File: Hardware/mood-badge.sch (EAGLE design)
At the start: 92 parts

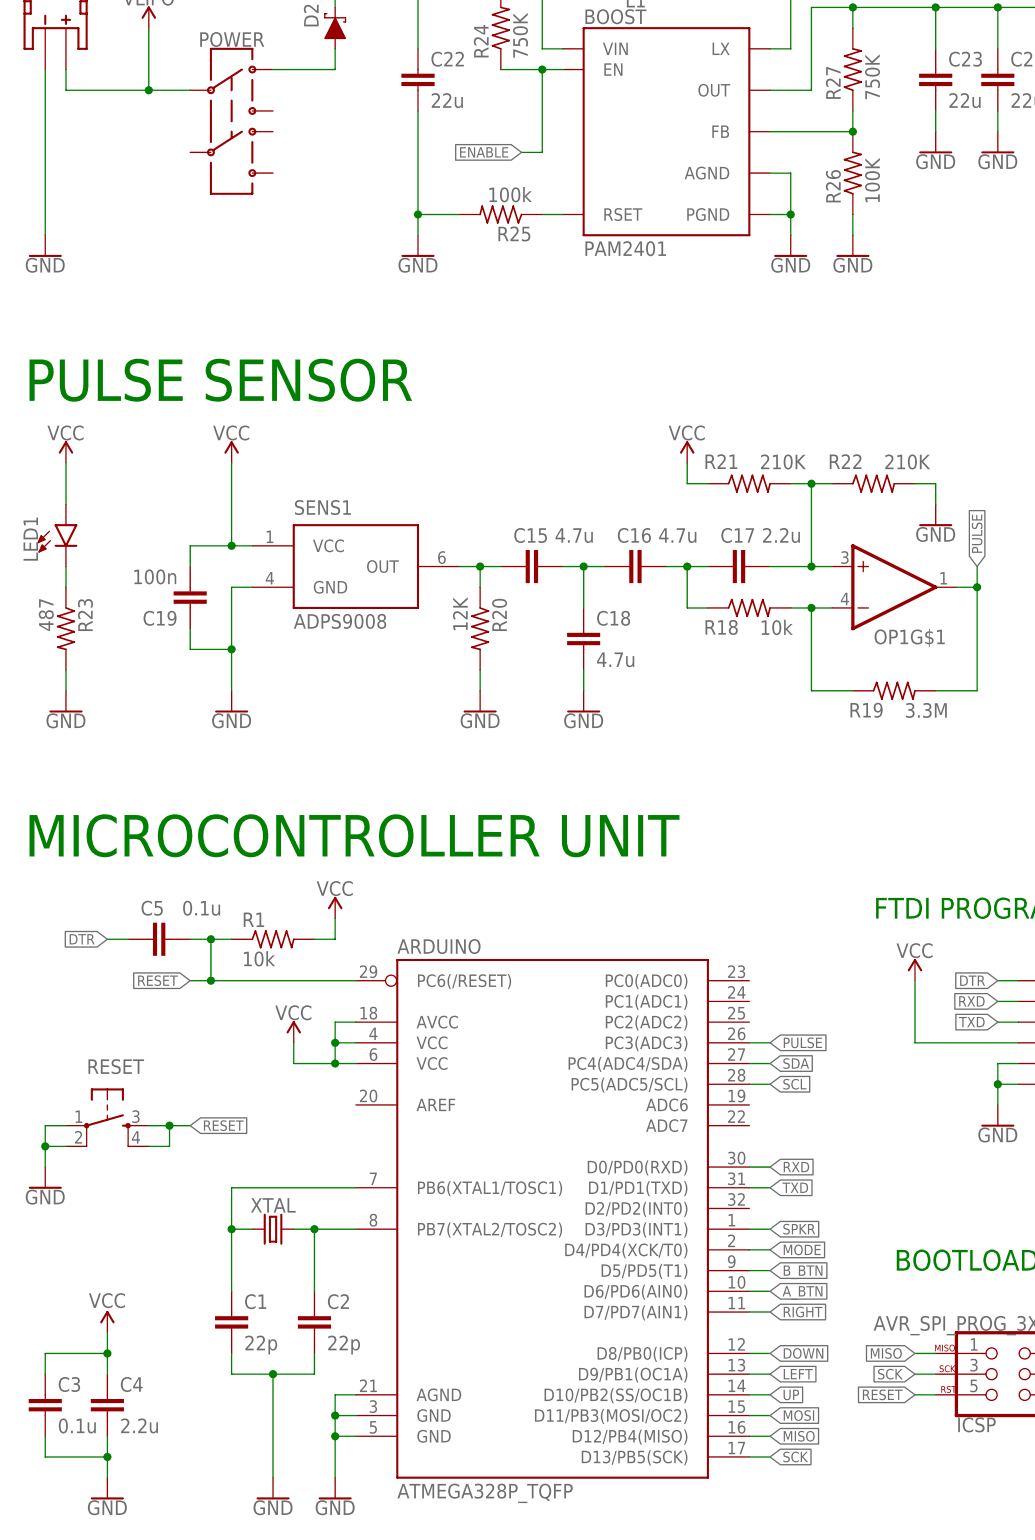
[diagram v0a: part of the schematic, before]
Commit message: Updated BOM, minor tweaks to part values
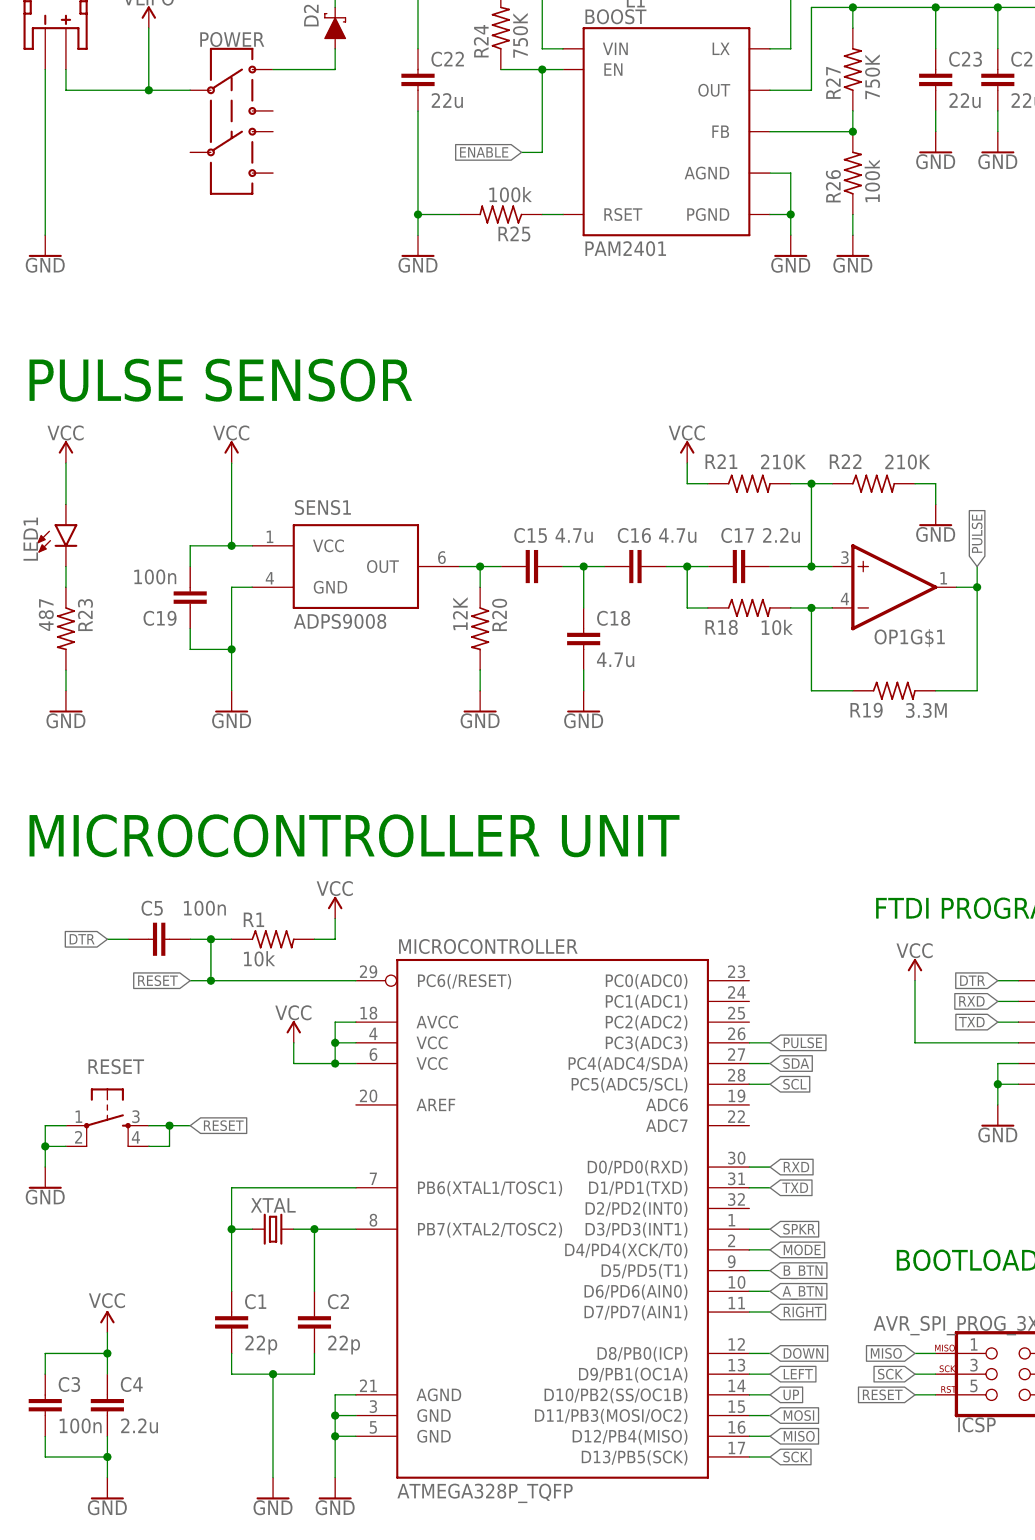
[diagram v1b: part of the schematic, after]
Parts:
- C3, C5: value 0.1u -> 100n
- R26: value 100K -> 100k
- renumbered ARDUINO to MICROCONTROLLER

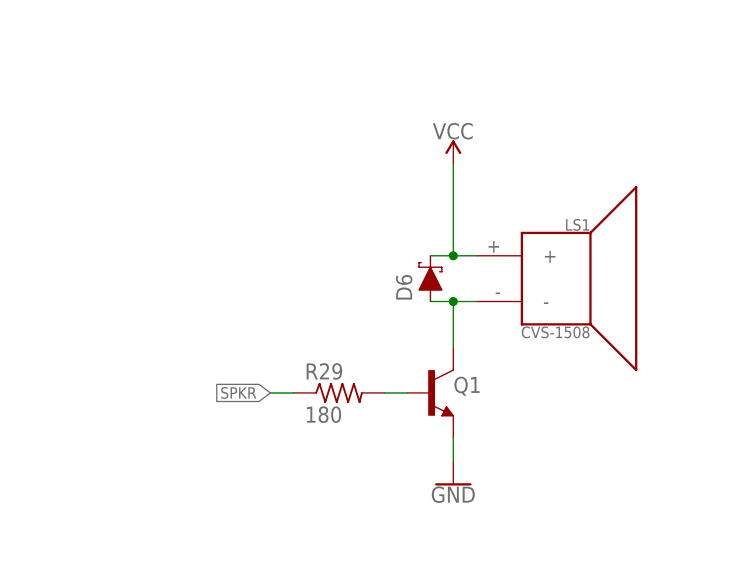
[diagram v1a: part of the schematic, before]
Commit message: Fixed diode numbering
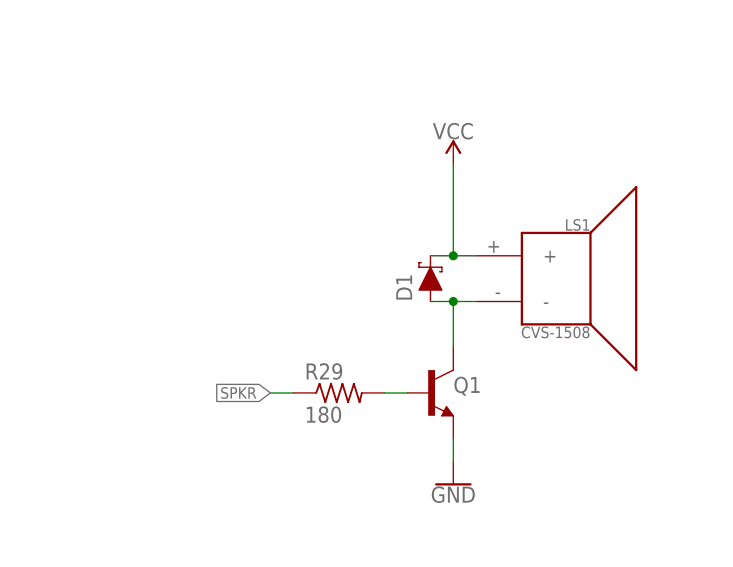
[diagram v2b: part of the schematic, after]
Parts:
- renumbered D6 to D1
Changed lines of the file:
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@@
 <part name="R29" library="LinnesLab-Passives" deviceset="RESISTOR" device="0603" package3d_urn="urn:adsk.eagle:package:15661944/2" value="180"/>
 <part name="GND38" library="LinnesLab-Symbols" deviceset="GND" device=""/>
-<part name="D6" library="LinnesLab-DiscreteSemi" deviceset="SCHOTTKY" device="-USC" package3d_urn="urn:adsk.eagle:package:15664784/2"/>
+<part name="D1" library="LinnesLab-DiscreteSemi" deviceset="SCHOTTKY" device="-USC" package3d_urn="urn:adsk.eagle:package:15664784/2"/>
 <part name="SUPPLY26" library="LinnesLab-Symbols" deviceset="VCC" device=""/>
 <part name="Q1" library="LinnesLab-DiscreteSemi" deviceset="NPN" device="-GENERIC" package3d_urn="urn:adsk.eagle:package:15662047/2"/>
@@
 <attribute name="VALUE" x="363.22" y="106.426" size="1.778" layer="96" align="top-center"/>
 </instance>
-<instance part="D6" gate="G$1" x="360.68" y="129.54" smashed="yes" rot="R90">
+<instance part="D1" gate="G$1" x="360.68" y="129.54" smashed="yes" rot="R90">
 <attribute name="NAME" x="358.648" y="127" size="1.778" layer="95" font="vector" rot="R90"/>
 <attribute name="VALUE" x="362.712" y="127" size="1.778" layer="96" font="vector" rot="R90" align="top-left"/>
@@
 </segment>
 <segment>
-<pinref part="D6" gate="G$1" pin="C"/>
+<pinref part="D1" gate="G$1" pin="C"/>
 <pinref part="LS1" gate="G$1" pin="+"/>
 <wire x1="360.68" y1="132.08" x2="363.22" y2="132.08" width="0.1524" layer="91"/>
@@
 <segment>
 <pinref part="LS1" gate="G$1" pin="-"/>
-<pinref part="D6" gate="G$1" pin="A"/>
+<pinref part="D1" gate="G$1" pin="A"/>
 <wire x1="365.76" y1="127" x2="363.22" y2="127" width="0.1524" layer="91"/>
 <pinref part="Q1" gate="G$1" pin="C"/>
